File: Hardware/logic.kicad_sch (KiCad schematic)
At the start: 80 parts, among them J1 USB_B_Micro, J301 Ref Divider, J302 GPS ANT, J303 Encoder, J304 Ref Select, J305 Ref Range, J306 GPS Module, J308 RF 50 Ohm, J309 RF TTL, J310 1PPS TTL, J311 ICSP, J312 Serial, J313 Program, J314 LCD, Q301 2N3904, U1 FT232RL, U301 DAC8571IDGK, U302 NEO-M8M, U303 OP07, U304 OP07, U305 TXS0108EPW, U306 GALI-52, U307 74LVC1G17, U308 74LVC1G17, U309 MCP23017_SO, U310 MAX232, U311 PIC18F27Q43, U312 24AA04

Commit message: changed uarts and lcd pins
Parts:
- removed J303: Encoder, Connector_PinSocket_2.54mm:PinSocket_1x06_P2.54mm_Vertical, symbol Connector:Conn_01x06_Pin
- removed J304: Ref Select, Connector_PinSocket_2.54mm:PinSocket_1x03_P2.54mm_Vertical, symbol Connector:Conn_01x03_Pin
- removed J305: Ref Range, Connector_PinSocket_2.54mm:PinSocket_1x03_P2.54mm_Vertical, symbol Connector:Conn_01x03_Pin
- removed J306: GPS Module, Connector_PinSocket_2.54mm:PinSocket_1x05_P2.54mm_Vertical, symbol Connector:Conn_01x05_Pin
- added C312: 4.7, symbol Device:C_Polarized_Small_US
- added C313, C314: 100n, Capacitor_THT:C_Axial_L3.8mm_D2.6mm_P15.00mm_Horizontal, symbol Device:C_US
- added D307: Green, LED_THT:LED_D3.0mm_Horizontal_O3.81mm_Z2.0mm, symbol Device:LED
- added D308, D311: Red, LED_THT:LED_D3.0mm_Horizontal_O3.81mm_Z2.0mm, symbol Device:LED
- added J303: GPS Module, symbol Connector_Generic:Conn_01x05
- added J306: VCO Range, symbol Connector_Generic:Conn_01x03
- added J307: Encoder, symbol Connector_Generic:Conn_01x06
- added J315: Ref Select, symbol Connector_Generic:Conn_01x03
- added R316: 4.7K, Resistor_THT:R_Axial_DIN0204_L3.6mm_D1.6mm_P7.62mm_Horizontal, symbol Device:R_US
- added R317: 10K, Resistor_THT:R_Axial_DIN0204_L3.6mm_D1.6mm_P7.62mm_Horizontal, symbol Device:R_US
- added R320, R322, R323: 330, Resistor_THT:R_Axial_DIN0204_L3.6mm_D1.6mm_P7.62mm_Horizontal, symbol Device:R_US
- D306: value LED -> Red
- D309, D312: value LED -> Green
- D310: value LED -> Yellow
- J1: value USB_B_Micro -> USB
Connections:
- net +5V: now also C312.1, C314.1, D307.2 (A), D308.2 (A), D311.2 (A), J303.1 (Pin_1), J307.2 (Pin_2)
- net 1PPS: now also J303.5 (Pin_5)
- net DCD: no longer J312.1
- net EXT_RX: now also U311.22 (RB1); no longer U311.24 (RB3)
- net EXT_TX: now also U311.21 (RB0); no longer U311.25 (RB4)
- net GND: now also U1.26 (TEST), C312.2, C313.2, C314.2, J303.2 (Pin_2), J307.6 (Pin_6), R317.2
- net GPS_RX: now also U311.26 (RB5), J303.4 (Pin_4); no longer U311.22 (RB1)
- net GPS_TX: now also U311.25 (RB4), J303.3 (Pin_3); no longer U311.21 (RB0)
- net INT: now also U311.7 (RA5); no longer U311.23 (RB2)
- net IntRef: now also J315.3 (Pin_3)
- net PGC: now also J313.1 (Pin_1)
- net PHASE-A: now also J307.1 (Pin_1)
- net PHASE-B: now also J307.3 (Pin_3)
- net RI: no longer J312.9
- net VCO: now also J306.2 (Pin_2)
- net VRef_FB: now also J315.1 (Pin_1)
- net ~{ENTER}: now also J307.5 (Pin_5)
- net ~{RESET}: no longer U1.19 (~{RESET})
- net at TP302.1, U301.2 (V_{REF}): now also J315.2 (Pin_2)
- net at R305.1, U304.6: now also J306.3 (Pin_3)
- net FAULT_N: now reaches U309.24 (GPA3)
- net FAULT_N: now also R323.2
- net at U301.3 (V_{SENSE}), U301.4 (V_{OUT}), U304.3 (+): now also J306.1 (Pin_1)
- net at J1.1 (VBUS): now also R316.1
- net at U1.17 (3V3OUT): now also C313.1
- net at U1.22 (CBUS1): now also R322.2
- net at U1.23 (CBUS0): now also R320.2
- new net: R316.2, R317.1, U1.19 (~{RESET})
- new net: D307.1 (K), R320.1
- new net: D311.1 (K), R323.1
- new net: D308.1 (K), R322.1
- new net USB_RX: U311.24 (RB3)
- new net USB_TX: U311.23 (RB2)
- no-connect marks 20 -> 35
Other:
- note added: "Fault"
- note added: "Install jumper to enable Bootloader and to download new software over external RS-232 link. Remove jumper for programming."
- note added: "Power - On when the system is operational Lock - OCXO RF is in phase/locked with GPS Holdover - GPS signal is lost and OCXO is free-running GPS - The GPS receiver has a 3D lock. Fault - On if any error condition is detected."
- note added: "USB RX"
- note added: "USB TX"
- note removed: "Power - On when the system is operational Lock - OCXO RF is in phase/locked with GPS Holdover - GPS signal is lost and OCXO is free-running GPS - The GPS receiver has a 3D lock."
- note removed: "Remove jumper to enable Bootloader and to download new software over external RS-232 link."
- moved on the sheet: C306, C307, D306, D309, D310, D312, J1, J311, J313, J314, Q301, R307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

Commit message: updated schematics
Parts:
- removed J311: ICSP, Connector_PinSocket_2.54mm:PinSocket_1x05_P2.54mm_Vertical, symbol Connector:Conn_01x05_Pin
- added J313: ICSP, symbol Connector_Generic:Conn_01x05
- renumbered C308 to C306, C310 to C307, C311 to C308, C314 to C310, C312 to C311, C306 to C312, C307 to C313, C313 to C314, D311 to D306, D306 to D307, D309 to D308, D310 to D309, D312 to D310, D313 to D311, D314 to D312, D307 to D313, D308 to D314, J307 to J303, J315 to J304, J306 to J305, J303 to J306, J314 to J307, J312 to J308, J308 to J309, J309 to J310, J310 to J311, J313 to J312, J1 to J314, R323 to R311, R315 to R312, R318 to R313, R319 to R314, R321 to R315, R311 to R316, R312 to R317, R313 to R318, R314 to R319, R322 to R321, R316 to R322, R317 to R323, TP302 to TP301, TP303 to TP302, TP305 to TP303, TP301 to TP305, U312 to U311, U311 to U312, U1 to U313
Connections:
- net +5V: now also J313.2 (Pin_2)
- net EXT_RX: no longer U313.5 (RXD)
- net EXT_TX: no longer U313.1 (TXD)
- net GND: now also J313.3 (Pin_3)
- net PGC: now also J313.5 (Pin_5)
- net PGD: now also J313.4 (Pin_4)
- net USB_RX: now also U313.5 (RXD)
- net USB_TX: now also U313.1 (TXD)
- net ~{MCLR}: now also J313.1 (Pin_1)
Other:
- note added: "Install jumper to enable Bootloader and to download new software over external USB link. Remove jumper for programming."
- note removed: "Install jumper to enable Bootloader and to download new software over external RS-232 link. Remove jumper for programming."

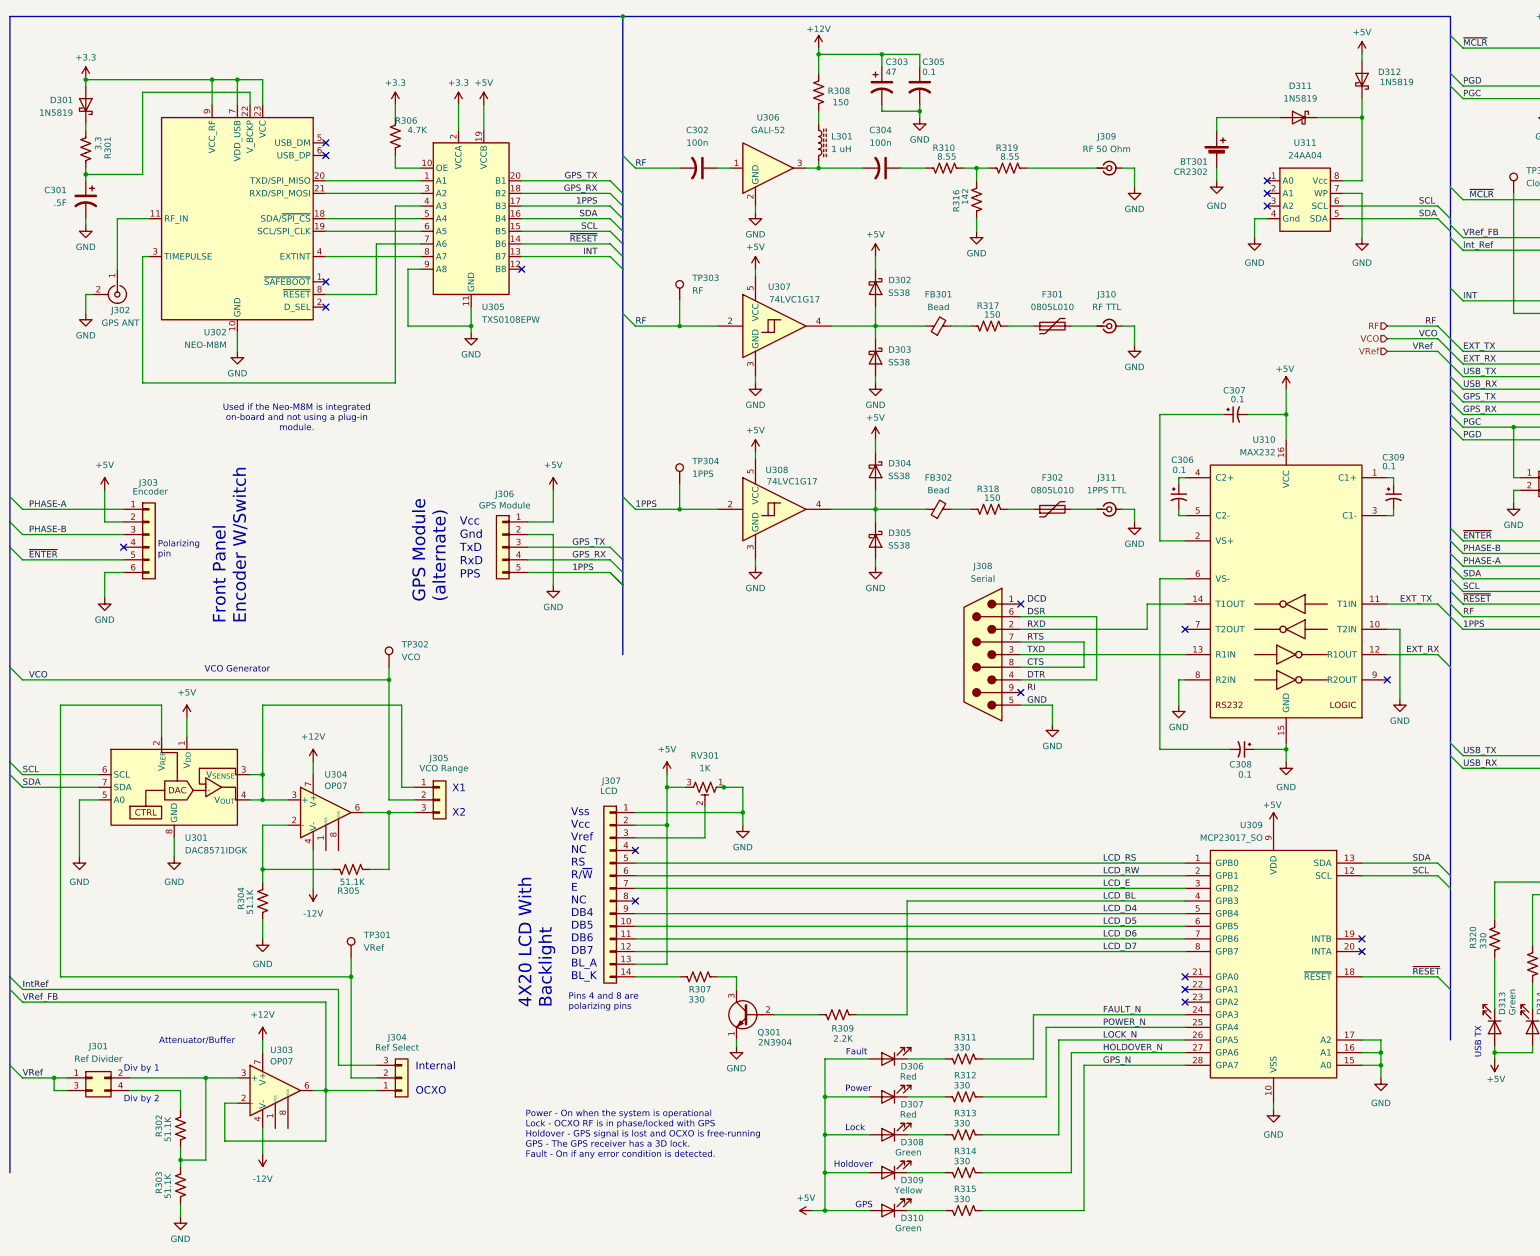
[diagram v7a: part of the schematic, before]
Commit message: updated schematics
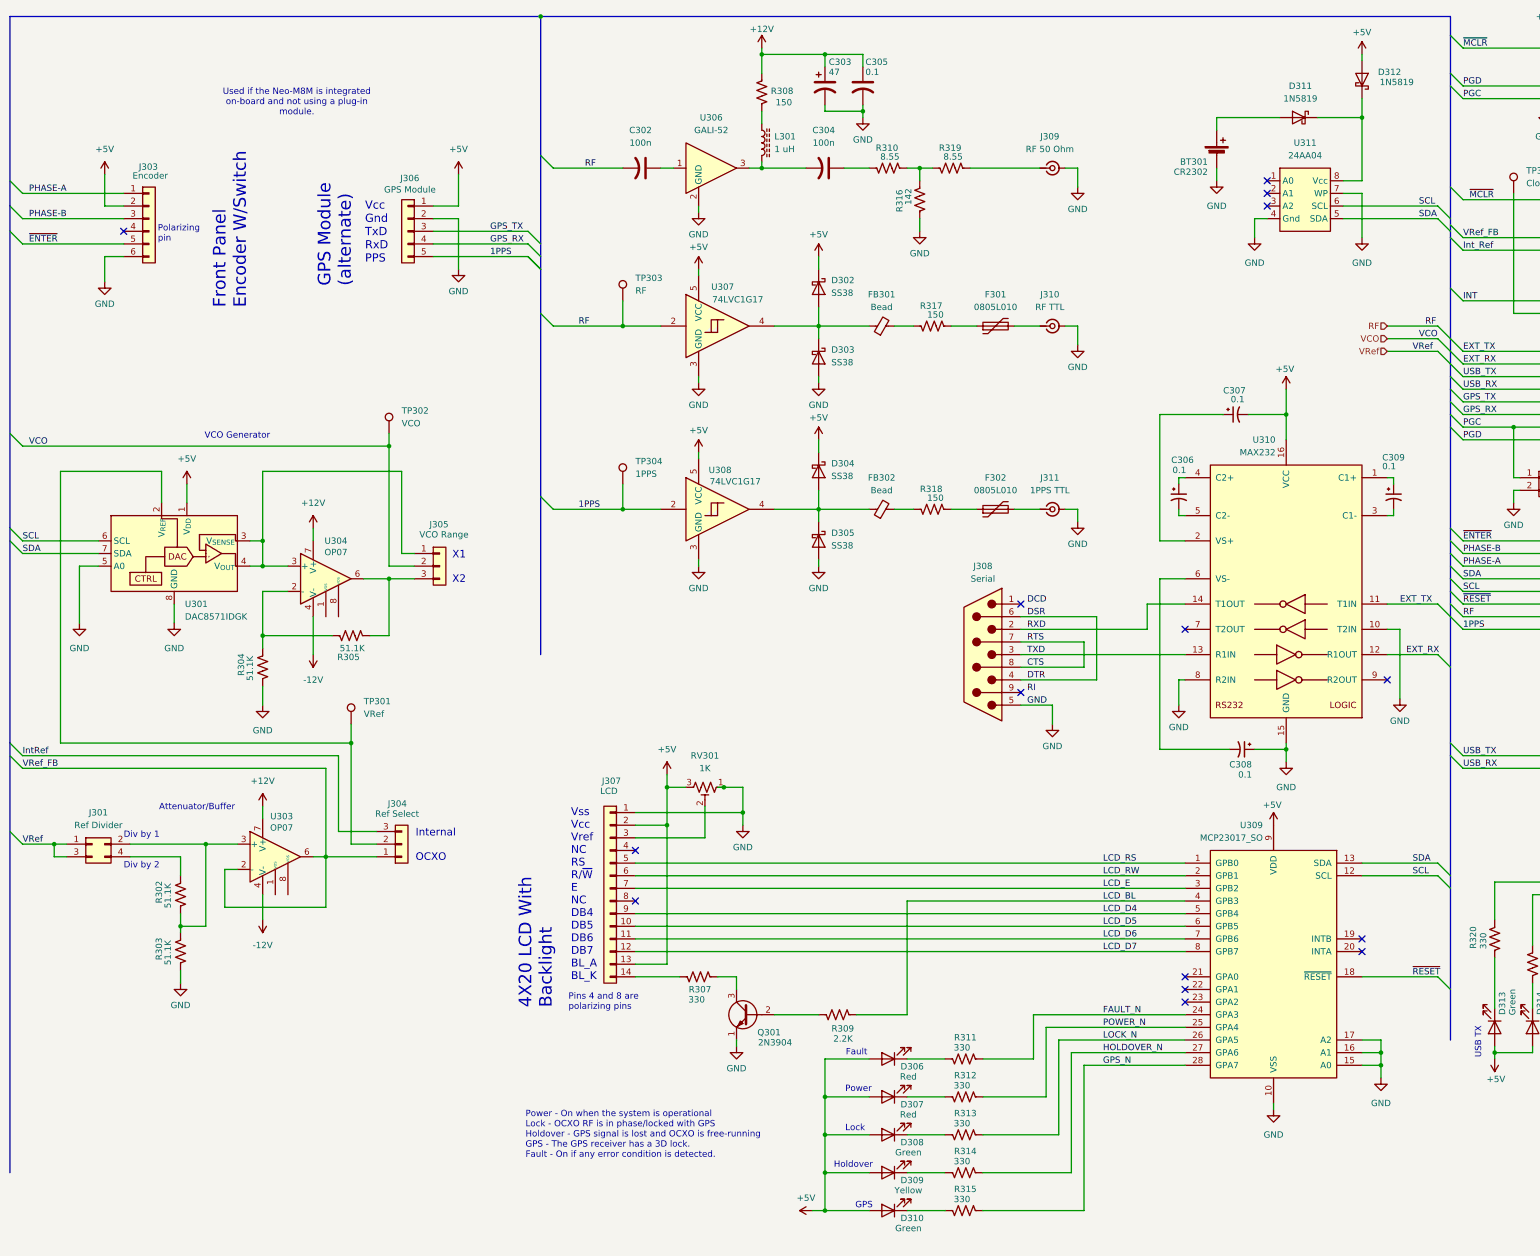
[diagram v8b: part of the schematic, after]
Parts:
- removed C301: .5F, Capacitor_THT:DX_5R5VxxxxU_D11.5mm_P5.00mm, symbol Device:C_Polarized_US
- removed D301: 1N5819, Diode_THT:D_DO-41_SOD81_P10.16mm_Horizontal, symbol Diode:1N5819
- removed J302: GPS ANT, Connector_Coaxial:SMA_Amphenol_901-144_Vertical, symbol Connector:Conn_Coaxial
- removed R301: 3.3, Resistor_THT:R_Axial_DIN0204_L3.6mm_D1.6mm_P7.62mm_Horizontal, symbol Device:R_US
- removed R306: 4.7K, Resistor_THT:R_Axial_DIN0207_L6.3mm_D2.5mm_P10.16mm_Horizontal, symbol Device:R_US
- removed U302: NEO-M8M, RF_GPS:ublox_NEO, symbol RF_GPS:NEO-M8M
- removed U305: TXS0108EPW, Package_SO:TSSOP-20_4.4x6.5mm_P0.65mm, symbol Logic_LevelTranslator:TXS0108EPW
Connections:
- no-connect marks 35 -> 30
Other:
- moved on the sheet: C302, C303, C304, C305, D302, D303, D304, D305, F301, F302, FB301, FB302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
